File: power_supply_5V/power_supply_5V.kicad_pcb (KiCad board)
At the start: 2 copper layers, 79 x 23 mm, 12 parts, among them J1 9-15V input DC, J2 +5V output, U1 L7805

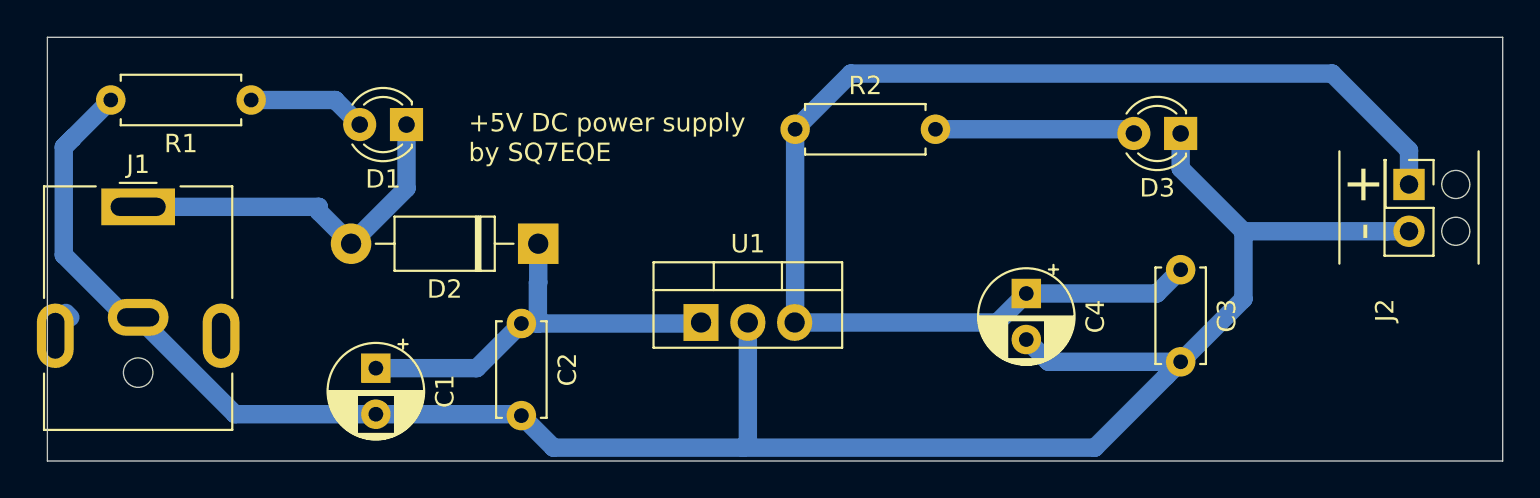
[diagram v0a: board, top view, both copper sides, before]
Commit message: update: I have prepared files for make own pcb
all Gerber files works fine with jlcpcb.com and others services
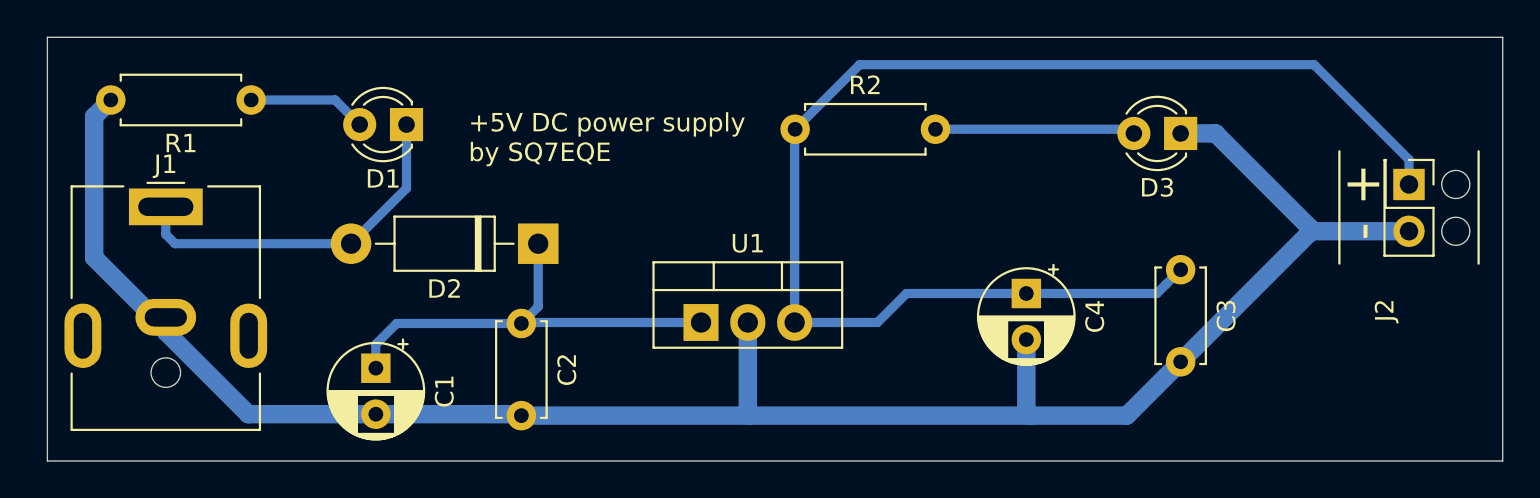
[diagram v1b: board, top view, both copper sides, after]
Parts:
- moved J1 1.50 mm to (80.1, 87.7)
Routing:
- net Net-(C1-Pad2): track 116.9 -> 107.1 mm
- net Net-(C1-Pad1): track 23.0 -> 24.2 mm
- net Net-(D1-Pad1): track 20.2 -> 19.5 mm
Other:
- net class Default: trace_width 0.25 -> 0.5
